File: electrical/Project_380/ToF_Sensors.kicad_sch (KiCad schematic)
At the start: 8 parts, among them J10 ToF 2, J11 ToF 3, J12 ToF 4, J13 IMU, J9 ToF 1, U3 TCA9548APWR

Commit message: added downforce motor control pin
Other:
- title: (none) -> Sensors
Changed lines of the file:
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@@
 (kicad_sch (version 20211123) (generator eeschema)
   (paper "A4")
+  (title_block
+    (title "Sensors")
+    (date "2022-02-03")
+    (rev "1.0")
+  )
   (junction (at 138.176 91.948) (diameter 0) (color 0 0 0 0)
   )

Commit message: added motor controller
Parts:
- R1, R2: footprint (none) -> Resistor_SMD:R_0603_1608Metric
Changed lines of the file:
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@@
       (effects (font (size 1.27 1.27)) (justify left))
     )
-    (property "Footprint" "" (id 2) (at 58.42 46.99 90)
+    (property "Footprint" "Resistor_SMD:R_0603_1608Metric" (id 2) (at 58.42 46.99 90)
       (effects (font (size 1.27 1.27)) hide)
     )
@@
   (symbol (lib_id "power:+3.3V") (at 61.976 39.878 0) (unit 1)
     (in_bom yes) (on_board yes) (fields_autoplaced)
-    (property "Reference" "#PWR?" (id 0) (at 61.976 43.688 0)
+    (property "Reference" "#PWR0115" (id 0) (at 61.976 43.688 0)
       (effects (font (size 1.27 1.27)) hide)
     )
@@
   (symbol (lib_id "power:+3.3V") (at 81.28 80.264 0) (unit 1)
     (in_bom yes) (on_board yes) (fields_autoplaced)
-    (property "Reference" "#PWR?" (id 0) (at 81.28 84.074 0)
+    (property "Reference" "#PWR0116" (id 0) (at 81.28 84.074 0)
       (effects (font (size 1.27 1.27)) hide)
     )
@@
   (symbol (lib_id "power:+3.3V") (at 125.222 54.102 0) (unit 1)
     (in_bom yes) (on_board yes) (fields_autoplaced)
-    (property "Reference" "#PWR?" (id 0) (at 125.222 57.912 0)
+    (property "Reference" "#PWR0117" (id 0) (at 125.222 57.912 0)
       (effects (font (size 1.27 1.27)) hide)
     )
@@
   (symbol (lib_id "power:GND") (at 138.176 108.966 0) (unit 1)
     (in_bom yes) (on_board yes) (fields_autoplaced)
-    (property "Reference" "#PWR?" (id 0) (at 138.176 115.316 0)
+    (property "Reference" "#PWR0119" (id 0) (at 138.176 115.316 0)
       (effects (font (size 1.27 1.27)) hide)
     )
@@
       (effects (font (size 1.27 1.27)) (justify left))
     )
-    (property "Footprint" "" (id 2) (at 67.564 46.99 90)
+    (property "Footprint" "Resistor_SMD:R_0603_1608Metric" (id 2) (at 67.564 46.99 90)
       (effects (font (size 1.27 1.27)) hide)
     )
@@
   (symbol (lib_id "power:GND") (at 110.49 112.014 0) (unit 1)
     (in_bom yes) (on_board yes) (fields_autoplaced)
-    (property "Reference" "#PWR?" (id 0) (at 110.49 118.364 0)
-      (effects (font (size 1.27 1.27)) hide)
-    )
+    (property "Reference" "#PWR0118" (id 0) (at 110.49 118.364 0)
+      (effects (font (size 1.27 1.27)) hide)
+    )

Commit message: Add design FOR THE RIGHT DONE GOT DANG PeeCeeBee
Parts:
- removed J13: IMU, symbol Connector:Conn_01x04_Female
- removed U3: TCA9548APWR, Package_SO:TSSOP-24_4.4x7.8mm_P0.65mm, symbol Interface_Expansion:TCA9548APWR
- added J13: IMU, Connector_PinHeader_2.54mm:PinHeader_1x10_P2.54mm_Vertical, symbol Connector:Conn_01x05_Female
- added U3, U6: NX3L4051PW,118, NX3L4051PW_118:SOP65P640X110-16N, symbol NX3L4051PW_118:NX3L4051PW,118
- J10, J11, J12, J9: footprint (none) -> Connector_JST:JST_XH_B4B-XH-A_1x04_P2.50mm_Vertical
- R1, R2: footprint Resistor_SMD:R_0603_1608Metric -> Resistor_SMD:R_0805_2012Metric_Pad1.20x1.40mm_HandSolder
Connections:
- net +3V3: now also J13.2 (Pin_2), U3.16 (VCC), U6.16 (VCC)
- net GND: now also J13.5 (Pin_5), U3.6 (~{E}), U3.8 (GND), U3.9 (S3), U6.6 (~{E}), U6.8 (GND), U6.9 (S3)
- net SCL: now also J13.3 (Pin_3), U3.3 (Z)
- net SDA: now also J13.4 (Pin_4), U6.3 (Z)
- net J9_SCL: now reaches J9.2 (Pin_2)
- net J9_SCL: now also U3.15 (Y2)
- net J9_SDA: now reaches J9.3 (Pin_3)
- net J9_SDA: now also U6.15 (Y2)
- net J12_SCL: now reaches J12.2 (Pin_2)
- net J12_SCL: now also U3.12 (Y3)
- net J12_SDA: now reaches J12.3 (Pin_3)
- net J12_SDA: now also U6.12 (Y3)
- net J10_SDA: now reaches J10.3 (Pin_3)
- net J10_SDA: now also U6.14 (Y1)
- net J10_SCL: now reaches J10.2 (Pin_2)
- net J10_SCL: now also U3.14 (Y1)
- net J11_SDA: now reaches J11.3 (Pin_3)
- net J11_SDA: now also U6.13 (Y0)
- net J11_SCL: now reaches J11.2 (Pin_2)
- net J11_SCL: now also U3.13 (Y0)
- new net S1: U3.11 (S1), U6.11 (S1)
- new net S2: U3.10 (S2), U6.10 (S2)
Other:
- moved on the sheet: J10, J11, J12, J9

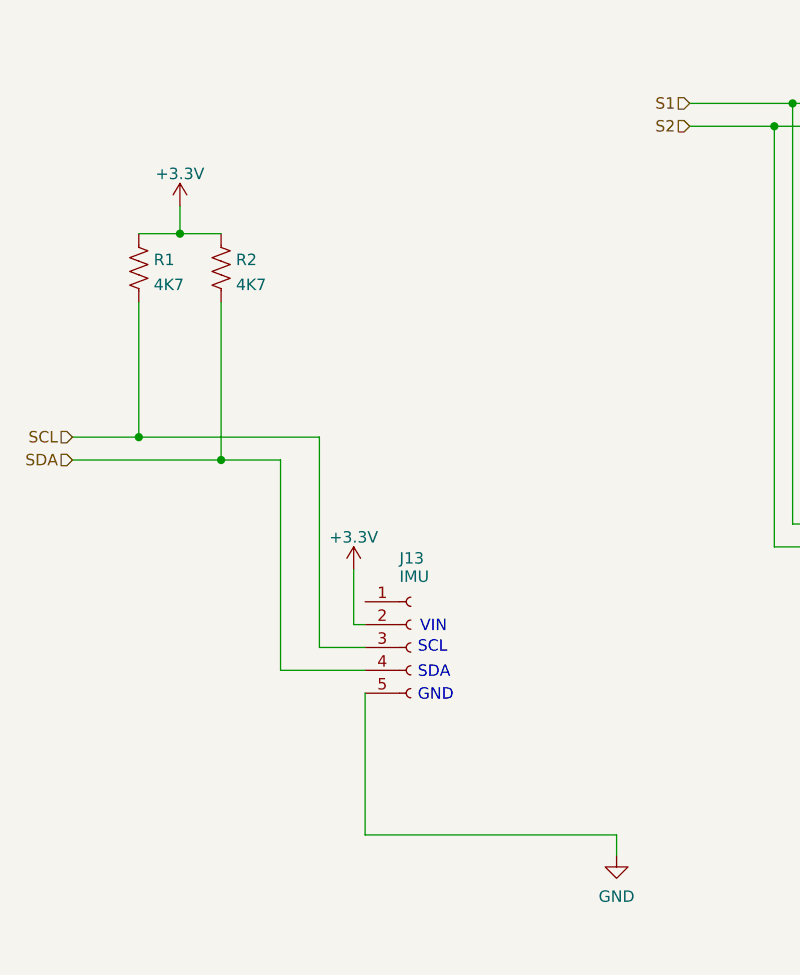
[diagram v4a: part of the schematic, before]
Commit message: Make fixes to board, add silkscreen, and generate gerbers
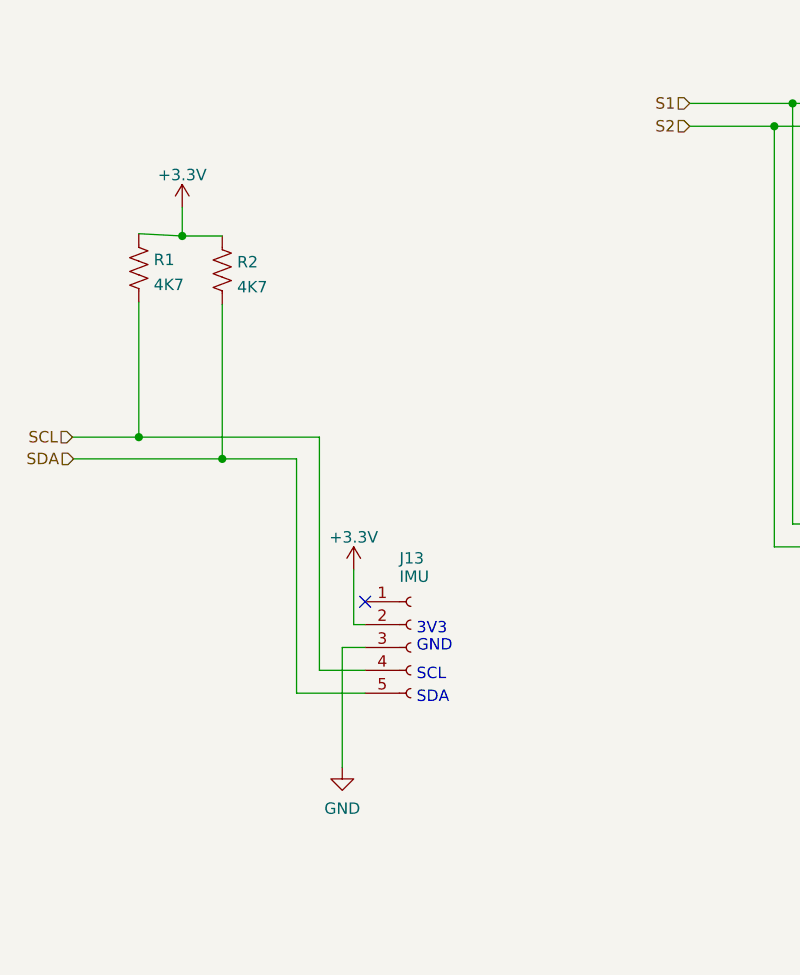
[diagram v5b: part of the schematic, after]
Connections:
- net GND: now also J13.3 (Pin_3); no longer J13.5 (Pin_5)
- net SCL: now also J13.4 (Pin_4); no longer J13.3 (Pin_3)
- net SDA: now also J13.5 (Pin_5); no longer J13.4 (Pin_4)
- no-connect marks 0 -> 1
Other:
- note removed: "VIN"
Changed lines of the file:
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@@
   (junction (at 236.982 100.33) (diameter 0) (color 0 0 0 0)
   )
-  (junction (at 61.976 42.926) (diameter 0) (color 0 0 0 0)
+  (junction (at 66.675 67.945) (diameter 0) (color 0 0 0 0)
+  )
+  (junction (at 62.23 43.18) (diameter 0) (color 0 0 0 0)
   )
   (junction (at 132.334 46.228) (diameter 0) (color 0 0 0 0)
@@
   (junction (at 128.016 30.988) (diameter 0) (color 0 0 0 0)
   )
-  (junction (at 66.548 68.072) (diameter 0) (color 0 0 0 0)
-  )
   (junction (at 132.334 92.964) (diameter 0) (color 0 0 0 0)
   )
@@
   (junction (at 57.404 65.532) (diameter 0) (color 0 0 0 0)
   )
+  (no_connect (at 82.55 83.82))
   (wire (pts (xy 162.814 28.448) (xy 165.354 28.448))
     (stroke (width 0) (type default) (color 0 0 0 0))
@@
     (stroke (width 0) (type default) (color 0 0 0 0))
   )
-  (wire (pts (xy 57.404 42.926) (xy 61.976 42.926))
+  (wire (pts (xy 57.404 42.926) (xy 62.23 43.18))
     (stroke (width 0) (type default) (color 0 0 0 0))
   )
@@
     (stroke (width 0) (type default) (color 0 0 0 0))
   )
-  (wire (pts (xy 50.038 68.072) (xy 66.548 68.072))
-    (stroke (width 0) (type default) (color 0 0 0 0))
-  )
   (wire (pts (xy 239.014 82.804) (xy 254.762 82.804))
     (stroke (width 0) (type default) (color 0 0 0 0))
@@
     (stroke (width 0) (type default) (color 0 0 0 0))
   )
-  (wire (pts (xy 110.49 109.728) (xy 110.49 112.014))
+  (wire (pts (xy 50.165 67.945) (xy 66.675 67.945))
     (stroke (width 0) (type default) (color 0 0 0 0))
   )
@@
     (stroke (width 0) (type default) (color 0 0 0 0))
   )
+  (wire (pts (xy 82.55 88.9) (xy 80.01 88.9))
+    (stroke (width 0) (type default) (color 0 0 0 0))
+  )
   (wire (pts (xy 162.814 75.184) (xy 165.862 75.184))
     (stroke (width 0) (type default) (color 0 0 0 0))
   )
-  (wire (pts (xy 82.55 91.44) (xy 73.152 91.44))
+  (wire (pts (xy 77.47 91.44) (xy 82.55 91.44))
     (stroke (width 0) (type default) (color 0 0 0 0))
   )
@@
     (stroke (width 0) (type default) (color 0 0 0 0))
   )
-  (wire (pts (xy 61.976 42.926) (xy 66.548 42.926))
+  (wire (pts (xy 62.23 43.18) (xy 66.675 43.18))
     (stroke (width 0) (type default) (color 0 0 0 0))
   )
@@
     (stroke (width 0) (type default) (color 0 0 0 0))
   )
+  (wire (pts (xy 66.675 50.8) (xy 66.675 67.945))
+    (stroke (width 0) (type default) (color 0 0 0 0))
+  )
   (wire (pts (xy 224.028 64.77) (xy 239.014 64.77))
     (stroke (width 0) (type default) (color 0 0 0 0))
@@
     (stroke (width 0) (type default) (color 0 0 0 0))
   )
+  (wire (pts (xy 74.93 93.98) (xy 82.55 93.98))
+    (stroke (width 0) (type default) (color 0 0 0 0))
+  )
   (wire (pts (xy 162.814 23.368) (xy 167.386 23.368))
     (stroke (width 0) (type default) (color 0 0 0 0))
@@
     (stroke (width 0) (type default) (color 0 0 0 0))
   )
-  (wire (pts (xy 73.152 91.44) (xy 73.152 68.072))
-    (stroke (width 0) (type default) (color 0 0 0 0))
-  )
-  (wire (pts (xy 77.47 88.9) (xy 77.47 65.532))
+  (wire (pts (xy 77.47 65.532) (xy 77.47 91.44))
     (stroke (width 0) (type default) (color 0 0 0 0))
   )
@@
     (stroke (width 0) (type default) (color 0 0 0 0))
   )
-  (wire (pts (xy 82.55 109.728) (xy 110.49 109.728))
-    (stroke (width 0) (type default) (color 0 0 0 0))
-  )
   (wire (pts (xy 239.014 82.804) (xy 239.014 92.71))
     (stroke (width 0) (type default) (color 0 0 0 0))
@@
     (stroke (width 0) (type default) (color 0 0 0 0))
   )
+  (wire (pts (xy 80.01 88.9) (xy 80.01 102.235))
+    (stroke (width 0) (type default) (color 0 0 0 0))
+  )
   (wire (pts (xy 167.386 23.368) (xy 167.386 20.828))
     (stroke (width 0) (type default) (color 0 0 0 0))
@@
     (stroke (width 0) (type default) (color 0 0 0 0))
   )
+  (wire (pts (xy 74.93 67.945) (xy 74.93 93.98))
+    (stroke (width 0) (type default) (color 0 0 0 0))
+  )
   (wire (pts (xy 254.762 90.424) (xy 236.982 90.424))
     (stroke (width 0) (type default) (color 0 0 0 0))
   )
-  (wire (pts (xy 66.548 68.072) (xy 73.152 68.072))
-    (stroke (width 0) (type default) (color 0 0 0 0))
-  )
   (wire (pts (xy 162.814 80.264) (xy 165.862 80.264))
     (stroke (width 0) (type default) (color 0 0 0 0))
   )
-  (wire (pts (xy 82.55 93.98) (xy 82.55 109.728))
-    (stroke (width 0) (type default) (color 0 0 0 0))
-  )
   (wire (pts (xy 254.762 109.982) (xy 236.982 109.982))
     (stroke (width 0) (type default) (color 0 0 0 0))
@@
     (stroke (width 0) (type default) (color 0 0 0 0))
   )
-  (wire (pts (xy 66.548 50.546) (xy 66.548 68.072))
-    (stroke (width 0) (type default) (color 0 0 0 0))
-  )
-  (wire (pts (xy 82.55 88.9) (xy 77.47 88.9))
-    (stroke (width 0) (type default) (color 0 0 0 0))
-  )
-  (wire (pts (xy 61.976 39.878) (xy 61.976 42.926))
+  (wire (pts (xy 62.23 40.005) (xy 62.23 43.18))
     (stroke (width 0) (type default) (color 0 0 0 0))
   )
@@
     (stroke (width 0) (type default) (color 0 0 0 0))
   )
+  (wire (pts (xy 66.675 67.945) (xy 74.93 67.945))
+    (stroke (width 0) (type default) (color 0 0 0 0))
+  )
   (wire (pts (xy 236.982 109.982) (xy 236.982 117.348))
     (stroke (width 0) (type default) (color 0 0 0 0))
@@
     (stroke (width 0) (type default) (color 0 0 0 0))
   )
-  (text "SDA" (at 88.392 92.456 0)
+  (text "SDA" (at 88.265 95.25 0)
     (effects (font (size 1.27 1.27)) (justify left bottom))
   )
@@
     (effects (font (size 1.27 1.27)) (justify left bottom))
   )
-  (text "GND\n" (at 88.392 94.996 0)
+  (text "GND\n" (at 88.265 89.535 0)
     (effects (font (size 1.27 1.27)) (justify left bottom))
   )
@@
     (effects (font (size 1.27 1.27)) (justify left bottom))
   )
-  (text "VIN\n" (at 88.646 87.376 0)
+  (text "3V3" (at 88.265 87.63 0)
     (effects (font (size 1.27 1.27)) (justify left bottom))
   )
@@
     (effects (font (size 1.27 1.27)) (justify left bottom))
   )
-  (text "SCL\n" (at 88.392 89.662 0)
+  (text "SCL\n" (at 88.265 92.71 0)
     (effects (font (size 1.27 1.27)) (justify left bottom))
   )
@@
     (effects (font (size 1.27 1.27)) (justify left))
   )
-  (hierarchical_label "SDA" (shape input) (at 50.038 68.072 180)
+  (hierarchical_label "SDA" (shape input) (at 50.165 67.945 180)
     (effects (font (size 1.27 1.27)) (justify right))
   )
@@
     (pin "2")
   )
-  (symbol (lib_id "power:+3.3V") (at 61.976 39.878 0) (unit 1)
-    (in_bom yes) (on_board yes) (fields_autoplaced)
-    (property "Reference" "#PWR0115" (id 0) (at 61.976 43.688 0)
-      (effects (font (size 1.27 1.27)) hide)
-    )
-    (property "Value" "+3.3V" (id 1) (at 61.976 36.2735 0))
-    (property "Footprint" "" (id 2) (at 61.976 39.878 0)
-      (effects (font (size 1.27 1.27)) hide)
-    )
-    (property "Datasheet" "" (id 3) (at 61.976 39.878 0)
+  (symbol (lib_id "power:+3.3V") (at 62.23 40.005 0) (unit 1)
+    (in_bom yes) (on_board yes) (fields_autoplaced)
+    (property "Reference" "#PWR0115" (id 0) (at 62.23 43.815 0)
+      (effects (font (size 1.27 1.27)) hide)
+    )
+    (property "Value" "+3.3V" (id 1) (at 62.23 36.4005 0))
+    (property "Footprint" "" (id 2) (at 62.23 40.005 0)
+      (effects (font (size 1.27 1.27)) hide)
+    )
+    (property "Datasheet" "" (id 3) (at 62.23 40.005 0)
       (effects (font (size 1.27 1.27)) hide)
     )
@@
     (pin "4")
   )
-  (symbol (lib_id "Device:R_US") (at 66.548 46.736 0) (unit 1)
-    (in_bom yes) (on_board yes) (fields_autoplaced)
-    (property "Reference" "R2" (id 0) (at 68.199 45.8275 0)
-      (effects (font (size 1.27 1.27)) (justify left))
-    )
-    (property "Value" "4K7" (id 1) (at 68.199 48.6026 0)
-      (effects (font (size 1.27 1.27)) (justify left))
-    )
-    (property "Footprint" "Resistor_SMD:R_0805_2012Metric_Pad1.20x1.40mm_HandSolder" (id 2) (at 67.564 46.99 90)
-      (effects (font (size 1.27 1.27)) hide)
-    )
-    (property "Datasheet" "~" (id 3) (at 66.548 46.736 0)
+  (symbol (lib_id "Device:R_US") (at 66.675 46.99 0) (unit 1)
+    (in_bom yes) (on_board yes) (fields_autoplaced)
+    (property "Reference" "R2" (id 0) (at 68.326 46.0815 0)
+      (effects (font (size 1.27 1.27)) (justify left))
+    )
+    (property "Value" "4K7" (id 1) (at 68.326 48.8566 0)
+      (effects (font (size 1.27 1.27)) (justify left))
+    )
+    (property "Footprint" "Resistor_SMD:R_0805_2012Metric_Pad1.20x1.40mm_HandSolder" (id 2) (at 67.691 47.244 90)
+      (effects (font (size 1.27 1.27)) hide)
+    )
+    (property "Datasheet" "~" (id 3) (at 66.675 46.99 0)
       (effects (font (size 1.27 1.27)) hide)
     )
@@
     (pin "2")
   )
-  (symbol (lib_id "power:GND") (at 110.49 112.014 0) (unit 1)
-    (in_bom yes) (on_board yes) (fields_autoplaced)
-    (property "Reference" "#PWR0118" (id 0) (at 110.49 118.364 0)
-      (effects (font (size 1.27 1.27)) hide)
-    )
-    (property "Value" "GND" (id 1) (at 110.49 116.5765 0))
-    (property "Footprint" "" (id 2) (at 110.49 112.014 0)
-      (effects (font (size 1.27 1.27)) hide)
-    )
-    (property "Datasheet" "" (id 3) (at 110.49 112.014 0)
-      (effects (font (size 1.27 1.27)) hide)
-    )
+  (symbol (lib_id "power:GND") (at 80.01 102.235 0) (unit 1)
+    (in_bom yes) (on_board yes) (fields_autoplaced)
+    (property "Reference" "#PWR0118" (id 0) (at 80.01 108.585 0)
+      (effects (font (size 1.27 1.27)) hide)
+    )
+    (property "Value" "GND" (id 1) (at 80.01 106.7975 0))
+    (property "Footprint" "" (id 2) (at 80.01 102.235 0)
+      (effects (font (size 1.27 1.27)) hide)
+    )
+    (property "Datasheet" "" (id 3) (at 80.01 102.235 0)
+      (effects (font (size 1.27 1.27)) hide)
+    )
